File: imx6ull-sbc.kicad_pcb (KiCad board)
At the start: 4 copper layers, 210 parts, among them J1 Micro_SD_Card_Det1, J2 USB4105, J3 USB1130, J4 USB4105, J5 Barrel_Jack_Switch, J6 CRJ011-ML3-TH, Q1 SiSA35DN, SW1 CAS-220TA, U1 MX6UL-VM, U10 SFEM064GB1ED1TO-I-6F-111-STD, U11 TPD4EUSB30, U12 74LVC1G06, U13 D5V0H1B2LP, U14 D5V0H1B2LP, U15 TPS54233, U16 TPS2116DRLR, U17 INA219BxD, U18 DP83825IRMQR, U2 MC32PF1510A6EP, U3 MT41K256M16, U4 TUSB320, U5 AP22814AW5, U6 TPD4EUSB30, U7 D5V0H1B2LP, U8 D5V0H1B2LP, U9 W25Q32JVZP, Y1 24Mhz, Y2 32.768kHz

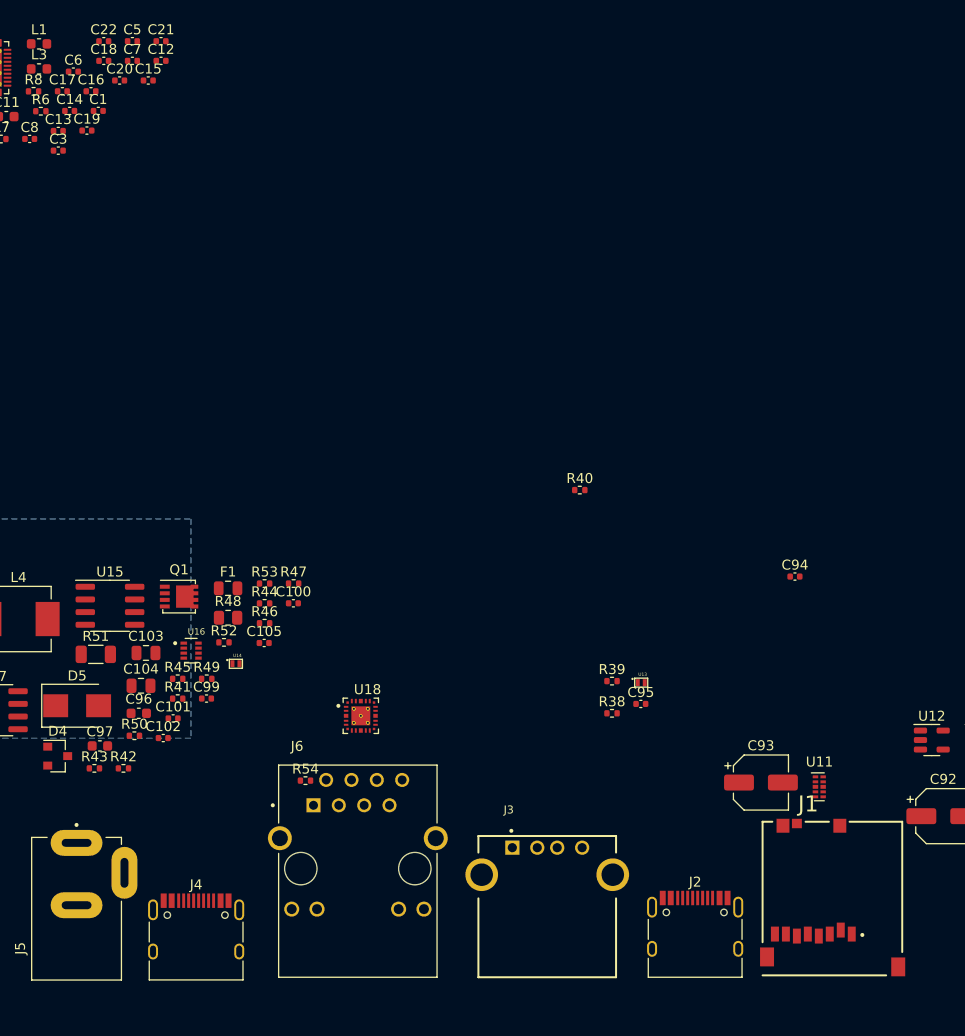
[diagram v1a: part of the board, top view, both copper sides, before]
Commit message: start moving to hierarchal labels, add emmc
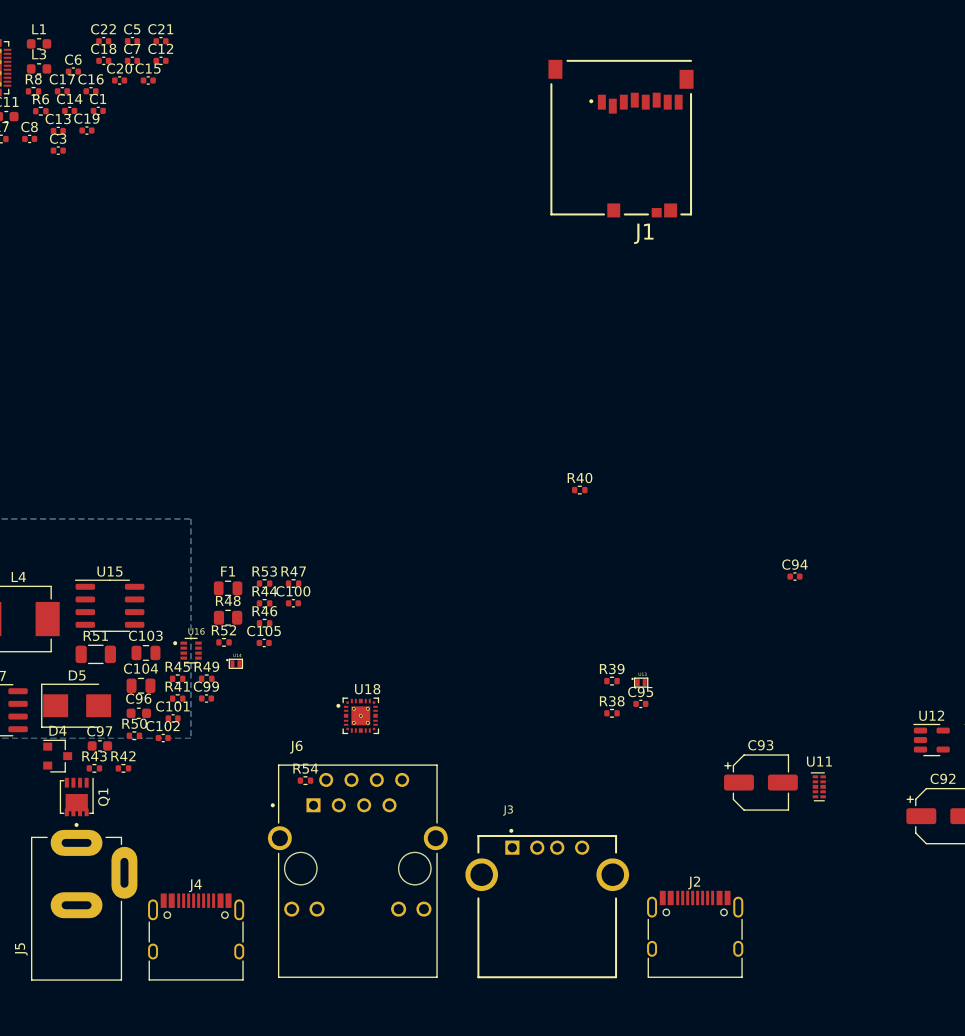
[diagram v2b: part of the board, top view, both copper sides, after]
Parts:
- moved J1 79.0 mm to (205.1, 40.9), turned to 180 degrees
- moved Q1 22.6 mm to (150.6, 106.9), turned to -90 degrees
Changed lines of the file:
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@@
   )
   (footprint "imx6ull-sbc:GCT_MEM2051-00-195-00-A_REVC" (layer "F.Cu")
-    (at 226.313008 116.96)
+    (at 205.1425 40.88 180)
     (property "DigiKey_PN" "2073-MEM2051-00-195-00-ACT-ND")
     (property "Sheetfile" "storage.kicad_sch")
@@
     (fp_line (start 7 7.8) (end 7 -7.6) (layer "F.Fab") (width 0.1))
     (fp_line (start -0.5 0) (end 0.5 0) (layer "F.Fab") (width 0.1))
-    (pad "1" smd rect (at 1.94 3.66) (size 0.8 1.5) (layers "F.Cu" "F.Paste" "F.Mask")
+    (pad "1" smd rect (at 1.94 3.66 180) (size 0.8 1.5) (layers "F.Cu" "F.Paste" "F.Mask")
       (net 9 "/Storage/SD1_DATA2") (pinfunction "DAT2") (pintype "bidirectional"))
-    (pad "2" smd rect (at 0.84 3.26) (size 0.8 1.5) (layers "F.Cu" "F.Paste" "F.Mask")
+    (pad "2" smd rect (at 0.84 3.26 180) (size 0.8 1.5) (layers "F.Cu" "F.Paste" "F.Mask")
       (net 10 "/Storage/SD1_DATA3") (pinfunction "DAT3/CD") (pintype "bidirectional"))
-    (pad "3" smd rect (at -0.26 3.66) (size 0.8 1.5) (layers "F.Cu" "F.Paste" "F.Mask")
+    (pad "3" smd rect (at -0.26 3.66 180) (size 0.8 1.5) (layers "F.Cu" "F.Paste" "F.Mask")
       (net 11 "/Storage/SD1_CMD") (pinfunction "CMD") (pintype "input"))
-    (pad "4" smd rect (at -1.36 3.86) (size 0.8 1.5) (layers "F.Cu" "F.Paste" "F.Mask")
+    (pad "4" smd rect (at -1.36 3.86 180) (size 0.8 1.5) (layers "F.Cu" "F.Paste" "F.Mask")
       (net 23 "DCDC_3V3") (pinfunction "VDD") (pintype "power_in"))
-    (pad "5" smd rect (at -2.46 3.66) (size 0.8 1.5) (layers "F.Cu" "F.Paste" "F.Mask")
+    (pad "5" smd rect (at -2.46 3.66 180) (size 0.8 1.5) (layers "F.Cu" "F.Paste" "F.Mask")
       (net 12 "/Storage/SD1_CLK") (pinfunction "CLK") (pintype "input"))
-    (pad "6" smd rect (at -3.56 3.86) (size 0.8 1.5) (layers "F.Cu" "F.Paste" "F.Mask")
+    (pad "6" smd rect (at -3.56 3.86 180) (size 0.8 1.5) (layers "F.Cu" "F.Paste" "F.Mask")
       (net 252 "GND") (pinfunction "VSS") (pintype "power_in"))
-    (pad "7" smd rect (at -4.66 3.66) (size 0.8 1.5) (layers "F.Cu" "F.Paste" "F.Mask")
+    (pad "7" smd rect (at -4.66 3.66 180) (size 0.8 1.5) (layers "F.Cu" "F.Paste" "F.Mask")
       (net 13 "/Storage/SD1_DATA0") (pinfunction "DAT0") (pintype "bidirectional"))
-    (pad "8" smd rect (at -5.76 3.66) (size 0.8 1.5) (layers "F.Cu" "F.Paste" "F.Mask")
+    (pad "8" smd rect (at -5.76 3.66 180) (size 0.8 1.5) (layers "F.Cu" "F.Paste" "F.Mask")
       (net 14 "/Storage/SD1_DATA1") (pinfunction "DAT1") (pintype "bidirectional"))
-    (pad "9" smd rect (at -4.95 -7.2) (size 1.3 1.4) (layers "F.Cu" "F.Paste" "F.Mask")
+    (pad "9" smd rect (at -4.95 -7.2 180) (size 1.3 1.4) (layers "F.Cu" "F.Paste" "F.Mask")
       (net 252 "GND") (pinfunction "SHIELD") (pintype "passive"))
-    (pad "9" smd rect (at 0.75 -7.2) (size 1.3 1.4) (layers "F.Cu" "F.Paste" "F.Mask")
+    (pad "9" smd rect (at 0.75 -7.2 180) (size 1.3 1.4) (layers "F.Cu" "F.Paste" "F.Mask")
       (net 252 "GND") (pinfunction "SHIELD") (pintype "passive"))
-    (pad "9" smd rect (at 6.6 6.95) (size 1.4 1.9) (layers "F.Cu" "F.Paste" "F.Mask")
+    (pad "9" smd rect (at 6.6 6.95 180) (size 1.4 1.9) (layers "F.Cu" "F.Paste" "F.Mask")
       (net 252 "GND") (pinfunction "SHIELD") (pintype "passive"))
-    (pad "9" smd rect (at -6.55 5.95) (size 1.4 1.9) (layers "F.Cu" "F.Paste" "F.Mask")
+    (pad "9" smd rect (at -6.55 5.95 180) (size 1.4 1.9) (layers "F.Cu" "F.Paste" "F.Mask")
       (net 252 "GND") (pinfunction "SHIELD") (pintype "passive"))
-    (pad "10" smd rect (at -3.56 -7.425) (size 1 0.95) (layers "F.Cu" "F.Paste" "F.Mask")
+    (pad "10" smd rect (at -3.56 -7.425 180) (size 1 0.95) (layers "F.Cu" "F.Paste" "F.Mask")
       (net 252 "GND") (pinfunction "DET") (pintype "output"))
     (model "${KIPRJMOD}/libraries/3dmodels/MEM2051-00-195-00-A_REVC.step"
@@
   )
   (footprint "Package_SO:Vishay_PowerPAK_1212-8_Single" (layer "F.Cu")
-    (at 160.82 86.79)
+    (at 150.56 106.88 -90)
     (descr "PowerPAK 1212-8 Single (https://www.vishay.com/docs/71656/ppak12128.pdf, https://www.vishay.com/docs/72597/72597.pdf)")
     (tags "Vishay PowerPAK 1212-8 Single")
@@
     (property "Sheetname" "VIN")
     (attr smd)
-    (fp_text reference "Q1" (at 0 -2.7) (layer "F.SilkS")
+    (fp_text reference "Q1" (at 0 -2.7 90) (layer "F.SilkS")
       (effects (font (size 1 1) (thickness 0.15)))
     )
-    (fp_text value "SiSA35DN" (at 0 2.7) (layer "F.Fab")
+    (fp_text value "SiSA35DN" (at 0 2.7 90) (layer "F.Fab")
       (effects (font (size 1 1) (thickness 0.15)))
     )
-    (fp_text user "${REFERENCE}" (at 0 0) (layer "F.Fab")
+    (fp_text user "${REFERENCE}" (at 0 0 90) (layer "F.Fab")
       (effects (font (size 0.7 0.7) (thickness 0.105)))
     )
@@
     (fp_line (start 1.525 -1.525) (end 1.525 1.525) (layer "F.Fab") (width 0.1))
     (fp_line (start -0.8 -1.525) (end 1.525 -1.525) (layer "F.Fab") (width 0.1))
-    (pad "1" smd rect locked (at -1.435 -0.99) (size 0.99 0.405) (layers "F.Cu" "F.Paste" "F.Mask")
+    (pad "1" smd rect locked (at -1.435 -0.99 270) (size 0.99 0.405) (layers "F.Cu" "F.Paste" "F.Mask")
       (net 234 "/VIN/JACK_VIN") (pinfunction "S") (pintype "passive"))
-    (pad "2" smd rect locked (at -1.435 -0.33) (size 0.99 0.405) (layers "F.Cu" "F.Paste" "F.Mask")
+    (pad "2" smd rect locked (at -1.435 -0.33 270) (size 0.99 0.405) (layers "F.Cu" "F.Paste" "F.Mask")
       (net 234 "/VIN/JACK_VIN") (pinfunction "S") (pintype "passive"))
-    (pad "3" smd rect locked (at -1.435 0.33) (size 0.99 0.405) (layers "F.Cu" "F.Paste" "F.Mask")
+    (pad "3" smd rect locked (at -1.435 0.33 270) (size 0.99 0.405) (layers "F.Cu" "F.Paste" "F.Mask")
       (net 234 "/VIN/JACK_VIN") (pinfunction "S") (pintype "passive"))
-    (pad "4" smd rect locked (at -1.435 0.99) (size 0.99 0.405) (layers "F.Cu" "F.Paste" "F.Mask")
+    (pad "4" smd rect locked (at -1.435 0.99 270) (size 0.99 0.405) (layers "F.Cu" "F.Paste" "F.Mask")
       (net 240 "Net-(C97-Pad2)") (pinfunction "G") (pintype "passive"))
-    (pad "5" smd custom locked (at 0.5575 0) (size 1.725 2.235) (layers "F.Cu" "F.Paste" "F.Mask")
+    (pad "5" smd custom locked (at 0.5575 0 270) (size 1.725 2.235) (layers "F.Cu" "F.Paste" "F.Mask")
       (net 220 "Net-(C96-Pad1)") (pinfunction "D") (pintype "passive") (zone_connect 2)
       (options (clearance outline) (anchor rect))
